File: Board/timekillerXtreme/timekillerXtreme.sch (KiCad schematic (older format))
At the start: 89 parts, among them J1 Battery, J10 Conn_01x02, J11 TP_USB, J12 PROG, J13 CONN_01X03, J14 TP_3.3V, J15 PE7, J16 PE8, J17 PE9, J18 PE10, J19 PD4, J2 USB_OTG, J20 PD1, J21 PD0, J22 PD3, J23 PE11, J24 Pb12, J3 Conn_Bottom_Expansion, J4 Conn_Internal_Expansion, J5 Conn_LCD_Board, J6 uSD, J7 CAPTEST, J8 TP_AUDIO_R, J9 TP_AUDIO_L, Q1 IRLML6302, Q2 PMBT3904.215, SW1 PWR, SW2 A, SW3 B, SW4 LEFT, SW5 RIGHT, SW6 DOWN, SW7 UP, SW8 RST, U1 MCP73831, U2 FT230XS-R, U3 NCP1529, U5 STM32F407VGT6, U6 USBLC6, U7 AOZ1310, U8 USBLC6, U9 USBLC6, Y1 32.768 KHz, Y2 16MHz

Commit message: Board: SD slot moved, usb-conn changed from slots to holes. LCD board polished. Repo cleaned up.
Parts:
- J2: footprint Connectors_USB:USB_Micro-B_Molex-105017-0001 -> timekiller-footprints:USB_Micro-B-CircularHoles
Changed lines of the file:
@@
 F 0 "J2" H 1000 14350 50  0000 L CNN
 F 1 "USB_OTG" H 1000 14250 50  0000 L CNN
-F 2 "Connectors_USB:USB_Micro-B_Molex-105017-0001" H 1350 13850 50  0001 C CNN
+F 2 "timekiller-footprints:USB_Micro-B-CircularHoles" H 1350 13850 50  0001 C CNN
 F 3 "" H 1350 13850 50  0001 C CNN
 	1    1200 13900

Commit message: Silkscreen fixed. Some minor tweaks.
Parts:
- J3: footprint Pin_Headers:Pin_Header_Angled_1x06_Pitch2.54mm -> timekiller-footprints:Pin_Header__1x06_Pitch2.54mm-NoSilk
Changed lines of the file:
@@
 F 0 "J3" H 13100 15450 50  0000 C CNN
 F 1 "Conn_Bottom_Expansion" H 13100 14750 50  0000 C CNN
-F 2 "Pin_Headers:Pin_Header_Angled_1x06_Pitch2.54mm" H 13100 15150 50  0001 C CNN
+F 2 "timekiller-footprints:Pin_Header__1x06_Pitch2.54mm-NoSilk" H 13100 15150 50  0001 C CNN
 F 3 "" H 13100 15150 50  0001 C CNN
 	1    13100 15150

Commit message: First round of modifications for rev.1
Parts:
- added C7: 100n, Capacitors_SMD:C_0805_HandSoldering, symbol C
- added J25: TP_BATT, Measurement_Points:Measurement_Point_Round-SMD-Pad_Small, symbol TEST_1P
- added R20, R21, R22, R23, R7: 47k, Resistors_SMD:R_0805_HandSoldering, symbol R
- C10, C9: value 4p -> 3.3p
- C11, C12: value 8p -> 8.2p
- C33: value 22u -> 2.2u
- D2: footprint Diodes_SMD:D_MiniMELF_Handsoldering -> Diodes_SMD:D_MiniMELF
- J6: symbol uSD -> uSD-RESCUE-timekillerXtreme
- R19: value 2k -> 0
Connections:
- net labels added: SYS_LED, VBATT_SENSE, VBUS_SENSE
- wire segments 494 -> 578
- no-connect marks 13 -> 12
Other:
- note added: "Batt to 3.3V reg\nNo undervoltage protection here"
- note added: "Bottom Expansion and its ESD protection"
- note added: "Buttons"
- note added: "Charging circuit"
- note added: "Internal expansion connector"
- note added: "LCD Backlight power switch"
- note added: "LCD board connector"
- note added: "Optional FTDI"
- note added: "SD card slot"
- note added: "ST-Link\nProgramming connector\nand debug serial"
- note added: "USB Connector"
- note removed: "Check the inductor footprint after it arrives!"
- note removed: "LCD connection modified!!\n"
- note removed: "Prog"
- note removed: "Verify touchscreen pinout!"
- moved on the sheet: C1, C10, C11, C12, C13, C16, C17, C19, C2, C22, C23, C28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

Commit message: Keeping repo up to date.
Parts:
- added F1: 1A, Resistors_SMD:R_0805_HandSoldering, symbol Fuse
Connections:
- net BATT+: now also F1.1; no longer J1.1 (Pin_1)
- net at J3.2 (Pin_2): now also U9.3 (I/O2)
- new net: F1.2, J1.1 (Pin_1)
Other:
- moved on the sheet: J3

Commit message: board & schematics updated
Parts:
- removed J15: PE7, Measurement_Points:Measurement_Point_Round-SMD-Pad_Small, symbol TEST_1P
- added C14, C21: 2.2u, Capacitors_SMD:C_0805_HandSoldering, symbol C
- added C15, C20: 100n, Capacitors_SMD:C_0805_HandSoldering, symbol C
- added C18: 4.7u, Capacitors_SMD:C_0805_HandSoldering, symbol C
- added C24: 100u, Capacitors_SMD:C_1210_HandSoldering, symbol C
- added R24: 10k, Resistors_SMD:R_0805_HandSoldering, symbol R
- added U4: TLV431, TO_SOT_Packages_SMD:TSOT-23, symbol TLV431
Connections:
- net +3V3: now also C14.1, C15.1, C18.2, C20.2, C21.1, C24.2, R24.1
- net GND: now also C14.2, C15.2, C18.1, C20.1, C21.2, C24.1, U4.2 (CATHODE)
- net VBUS_SENSE: now also U5.38 (PE7); no longer U5.36 (PB1)
- new net: R24.2, U4.3 (ANODE)
- new net 1.2VREF: U4.1 (REF), U5.36 (PB1)
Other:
- note added: "Batt to 3.3V reg\nNCP1529 will cut of at 2.4V"
- note added: "Board Revision detection\nRev1: Both pins are floating\nRev2: BoardRevDetect1 is connected to 3.3V\n BoardRevDetect2 is floating"
- note added: "Ian is set to about 200uA"
- note removed: "Batt to 3.3V reg\nNo undervoltage protection here"
- note removed: "Board Revision detection\nRev0: Both pins are floating"
- moved on the sheet: C17, C3, C4, C5, C6, D1, D2, D4, F1, J1, J10, J11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

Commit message: Case and board updated, this will be shipped to the boardhouse and I will call it rev2 if it is ok.
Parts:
- added VREF: VREF, Measurement_Points:Measurement_Point_Round-SMD-Pad_Small, symbol TEST_1P
- Q1, Q2: footprint TO_SOT_Packages_SMD:SOT-23 -> TO_SOT_Packages_SMD:SOT-23_Handsoldering
- U1, U3: footprint TO_SOT_Packages_SMD:SOT-23-5 -> TO_SOT_Packages_SMD:SOT-23-5_HandSoldering
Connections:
- net 1.2VREF: now also VREF.1

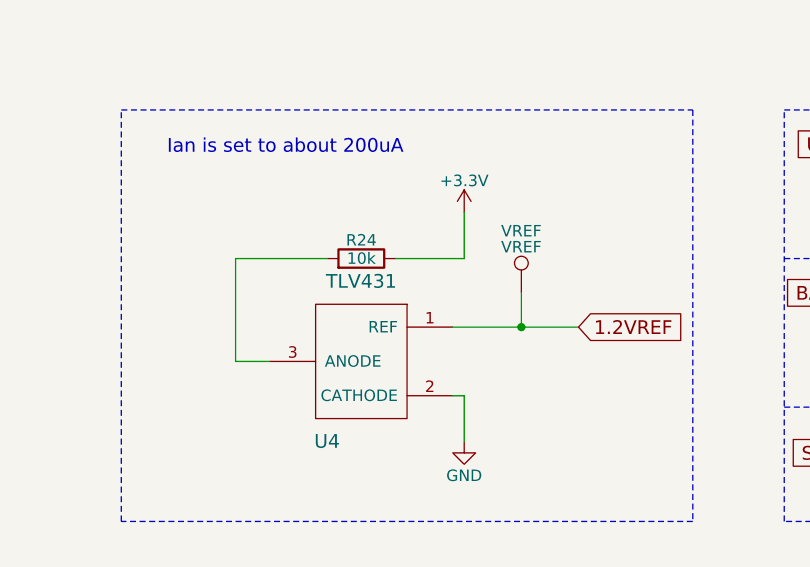
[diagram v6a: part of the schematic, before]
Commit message: Vref fixed, board was sent to boardhouse.
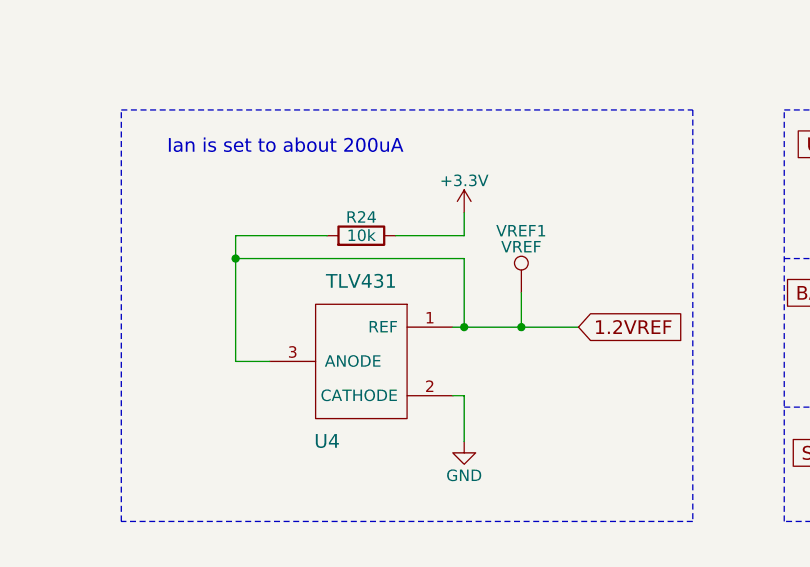
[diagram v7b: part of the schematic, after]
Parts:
- renumbered VREF to VREF1
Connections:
- net 1.2VREF: now also R24.2, U4.3 (ANODE)
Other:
- moved on the sheet: R24
